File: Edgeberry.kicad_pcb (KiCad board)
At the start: 2 copper layers, 135 x 90 mm, 171 parts, among them J1 Molex_KK_1x02_P2.54mm_CONN, P1 Barrel_Jack_CONN, Q1 BC547, Q2 BC547, Q3 BC547, SW1 SW_PUSH_Horizontal, U1 24LC256, U2 LM2596S-5.0

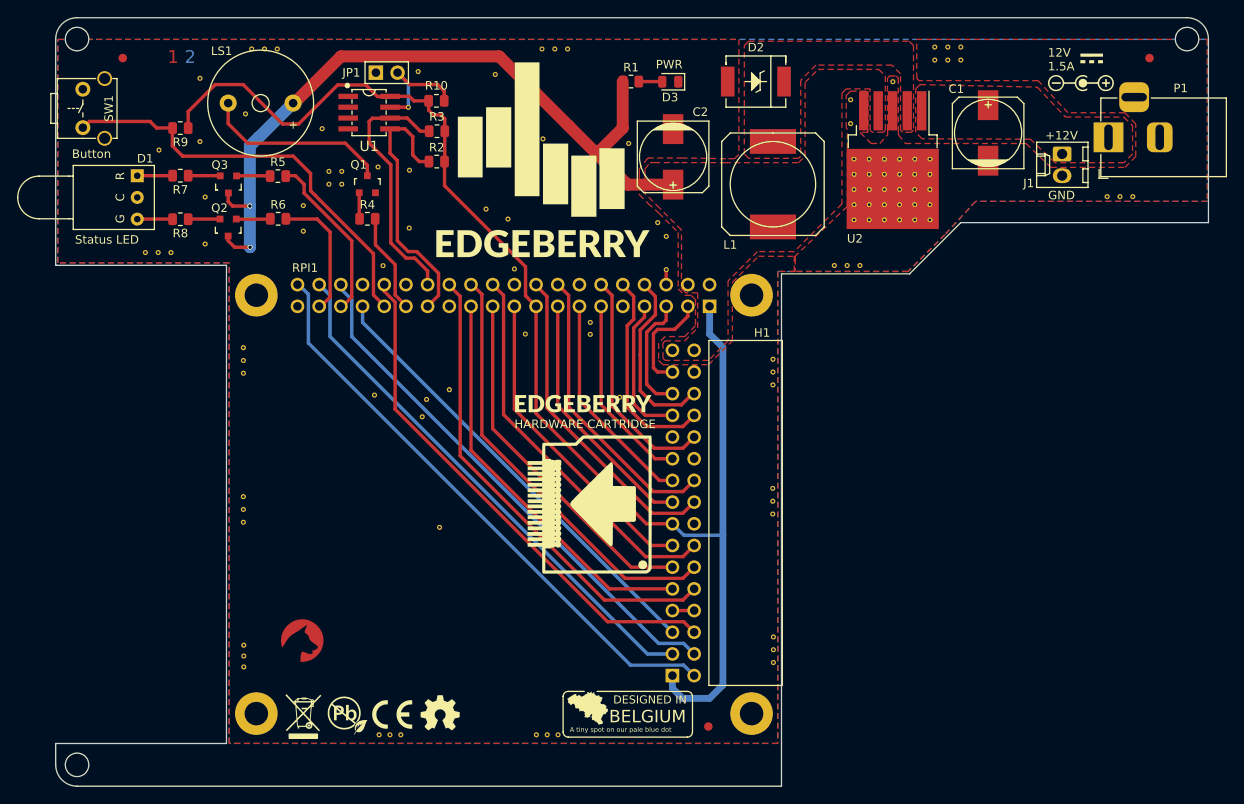
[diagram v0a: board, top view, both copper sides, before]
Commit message: Bugfix RPi footprint + via's are via's now instead footprints. KiCad * update.
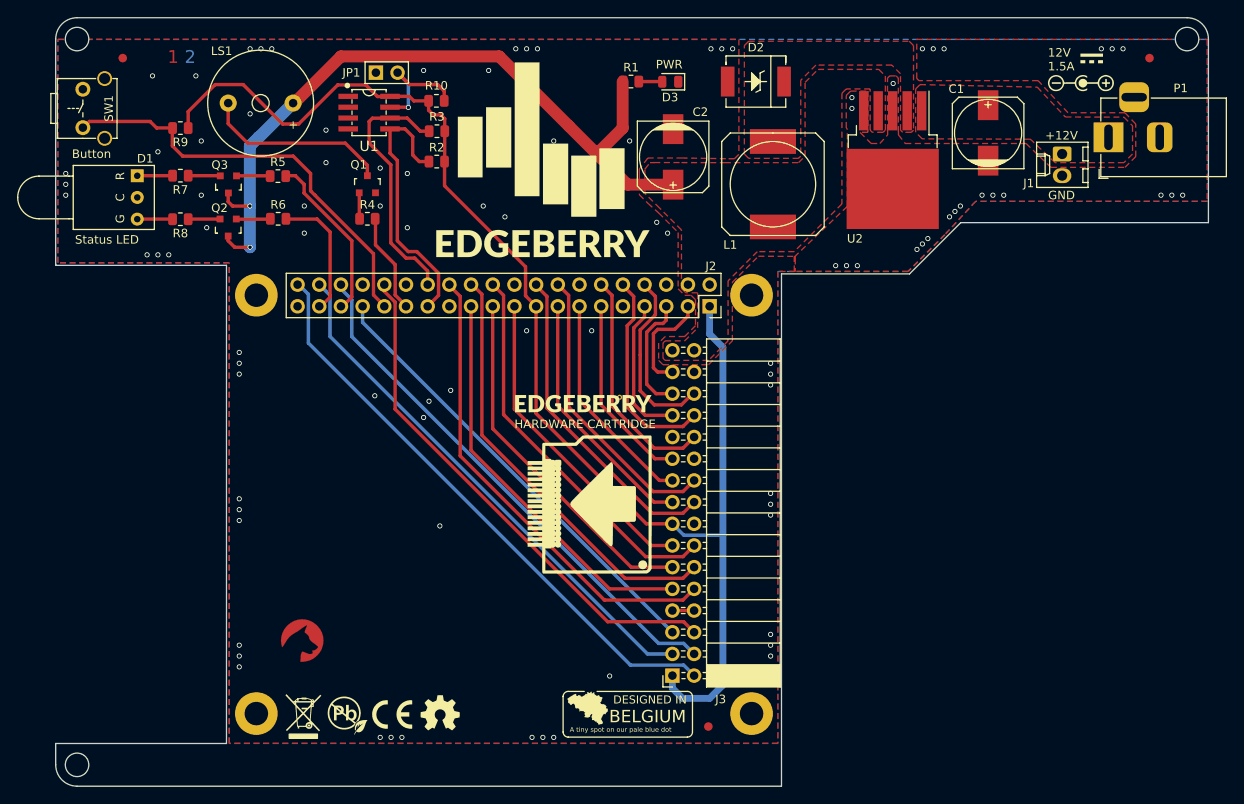
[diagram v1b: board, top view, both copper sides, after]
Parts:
- removed ? (x3): , 
- removed H1: 2X16Pin_P2.54mm_Horizontal_Receptacle_Connector, emcosys:EdgeBerry_IO
- removed the REF** at (114.8, 64.8)
- removed the REF** at (139.9, 135.8)
- removed the REF** at (128.6, 111.5)
- removed the REF** at (115.6, 69.8)
- removed the REF** at (141.2, 135.8)
- removed the REF** at (125.1, 76.4)
- removed the REF** at (121.0, 96.0)
- removed the REF** at (154.1, 75.8)
- removed the REF** at (105.6, 90.4)
- removed the REF** at (177.8, 80.8)
- removed the REF** at (105.6, 109.4)
- removed the REF** at (105.7, 125.3)
- removed the REF** at (105.7, 126.5)
- removed the REF** at (167.7, 127.3)
- removed the REF** at (121.5, 135.8)
- removed the REF** at (124.1, 135.8)
- removed the REF** at (135.1, 58.4)
- removed the REF** at (167.7, 124.3)
- removed the REF** at (105.7, 127.8)
- removed the REF** at (138.6, 88.8)
- removed the REF** at (181.7, 59.3)
- removed the REF** at (167.7, 125.8)
- removed the REF** at (122.8, 135.8)
- removed the REF** at (174.8, 80.8)
- removed the REF** at (105.6, 107.9)
- removed the REF** at (176.3, 80.8)
- removed the REF** at (105.6, 110.9)
- removed the REF** at (112.6, 73.8)
- removed the REF** at (178.9, 73.7)
- removed the REF** at (105.6, 91.9)
- removed the REF** at (178.9, 75.4)
- removed the REF** at (177.1, 70.1)
- removed the REF** at (177.1, 75.4)
- removed the REF** at (180.7, 68.3)
- removed the REF** at (100.5, 58.9)
- removed the REF** at (182.5, 68.3)
- removed the REF** at (176.7, 64.2)
- removed the REF** at (101.1, 78.3)
- removed the REF** at (186.0, 73.7)
- removed the REF** at (177.1, 71.9)
- removed the REF** at (177.1, 73.7)
- removed the REF** at (180.7, 71.9)
- removed the REF** at (186.0, 71.9)
- removed the REF** at (136.6, 75.4)
- removed the REF** at (155.1, 81.3)
- removed the REF** at (184.3, 73.7)
- removed the REF** at (182.5, 70.1)
- removed the REF** at (178.9, 70.1)
- removed the REF** at (182.5, 73.7)
- removed the REF** at (178.9, 68.3)
- removed the REF** at (122.0, 80.8)
- removed the REF** at (180.7, 70.1)
- removed the REF** at (180.7, 75.4)
- removed the REF** at (184.3, 75.4)
- removed the REF** at (117.1, 71.3)
- removed the REF** at (117.1, 69.8)
- removed the REF** at (184.3, 70.1)
- removed the REF** at (178.9, 71.9)
- removed the REF** at (142.1, 55.4)
- removed the REF** at (182.5, 71.9)
- removed the REF** at (209.8, 72.7)
- removed the REF** at (127.1, 96.5)
- removed the REF** at (186.6, 56.7)
- removed the REF** at (176.7, 61.4)
- removed the REF** at (143.6, 55.4)
- removed the REF** at (186.0, 70.1)
- removed the REF** at (109.6, 55.4)
- removed the REF** at (188.1, 56.7)
- removed the REF** at (112.6, 76.8)
- removed the REF** at (146.3, 87.5)
- removed the REF** at (186.0, 68.3)
- removed the REF** at (186.6, 55.2)
- removed the REF** at (208.3, 72.7)
- removed the REF** at (115.6, 71.3)
- removed the REF** at (121.4, 69.3)
- removed the REF** at (189.6, 56.7)
- removed the REF** at (184.3, 68.3)
- removed the REF** at (126.6, 98.5)
- removed the REF** at (146.3, 88.9)
- removed the REF** at (184.3, 71.9)
- removed the REF** at (129.8, 95.3)
- removed the REF** at (95.7, 67.3)
- removed the REF** at (189.6, 55.2)
- removed the REF** at (177.1, 68.3)
- removed the REF** at (188.1, 55.2)
- removed the REF** at (182.5, 75.4)
- removed the REF** at (180.7, 73.7)
- removed the REF** at (186.0, 75.4)
- removed the REF** at (101.1, 72.8)
- removed the REF** at (105.6, 93.4)
- removed the REF** at (167.6, 91.8)
- removed the REF** at (140.6, 55.4)
- removed the REF** at (137.4, 81.2)
- removed the REF** at (94.1, 79.3)
- removed the REF** at (95.6, 79.3)
- removed the REF** at (140.7, 66.0)
- removed the REF** at (206.8, 72.7)
- removed the REF** at (100.5, 66.3)
- removed the REF** at (167.6, 108.4)
- removed the REF** at (167.6, 106.9)
- removed the REF** at (167.6, 109.9)
- removed the REF** at (97.1, 79.3)
- removed the REF** at (167.6, 94.8)
- removed the REF** at (167.6, 93.3)
- removed the REF** at (105.9, 63.0)
- removed the REF** at (142.5, 135.8)
- removed the REF** at (106.6, 55.4)
- removed the REF** at (108.1, 55.4)
- removed the REF** at (125.1, 69.6)
- removed the REF** at (155.2, 77.4)
- removed the REF** at (134.0, 74.2)
- removed RPI1: 2X20Pin_2.54mm_Receptacle_CONN, emcosys:RPI_GPIO
- added J2: Raspberry_Pi_2_3, Connector_PinSocket_2.54mm:PinSocket_2x20_P2.54mm_Vertical, F.Cu at (160.2, 85.6)
- added J3: Edgeberry Cartridge Connector, Connector_PinSocket_2.54mm:PinSocket_2x16_P2.54mm_Horizontal, F.Cu at (155.9, 128.8)
- J1: value Molex_KK_1x02_P2.54mm_CONN -> Molex_KK_1x02_P2.54mm
- P1: value Barrel_Jack_CONN -> 12Vin
- SW1: value SW_PUSH_Horizontal -> SW_PUSH
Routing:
- net GND: track 5.50 -> 2.54 mm, vias 0 -> 94
- net GPIO_27: track 26.5 -> 25.8 mm
- net GPIO_22: track 30.4 -> 29.8 mm
- net LED_red: track 20.3 -> 19.8 mm
- net LED_green: track 15.7 -> 15.2 mm
- net WP: vias 0 -> 1
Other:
- board text added: "REV 1.5"
- board text added: "REV.: 1.5, Mid 2024"
- board text removed: "REV 1.4"
- board text removed: "REV.: 1.4, Mid 2024"

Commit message: Open Source Hardware license: CERN-OHL-W
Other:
- board text added: "Copyright© 2024 Sanne 'SpuQ' Santens. This design is released under the CERN OHL-W license on GitHub."
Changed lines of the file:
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@@
 		)
 		(fp_text user "${REFERENCE}"
-			(at -8.315 19.05 270)
+			(at -8.315 19.05 -90)
 			(layer "F.Fab")
 			(effects
@@
 	)
 	(gr_text "Edgeberry Hardware"
-		(at 72.449 29.072 0)
+		(at 72.449 19.772 0)
 		(layer "Dwgs.User")
 		(effects
@@
 	)
 	(gr_text "REV.: 1.5, Mid 2024"
-		(at 72.949 36.572 0)
+		(at 72.949 26.772 0)
 		(layer "Dwgs.User")
 		(effects
@@
 		)
 	)
+	(gr_text "Copyright© 2024 Sanne 'SpuQ' Santens. This design is released under\nthe CERN OHL-W license on GitHub."
+		(at 73.309 33.772 0)
+		(layer "Dwgs.User")
+		(effects
+			(font
+				(size 1.5 1.5)
+				(thickness 0.2)
+				(bold yes)
+			)
+			(justify left bottom)
+		)
+	)

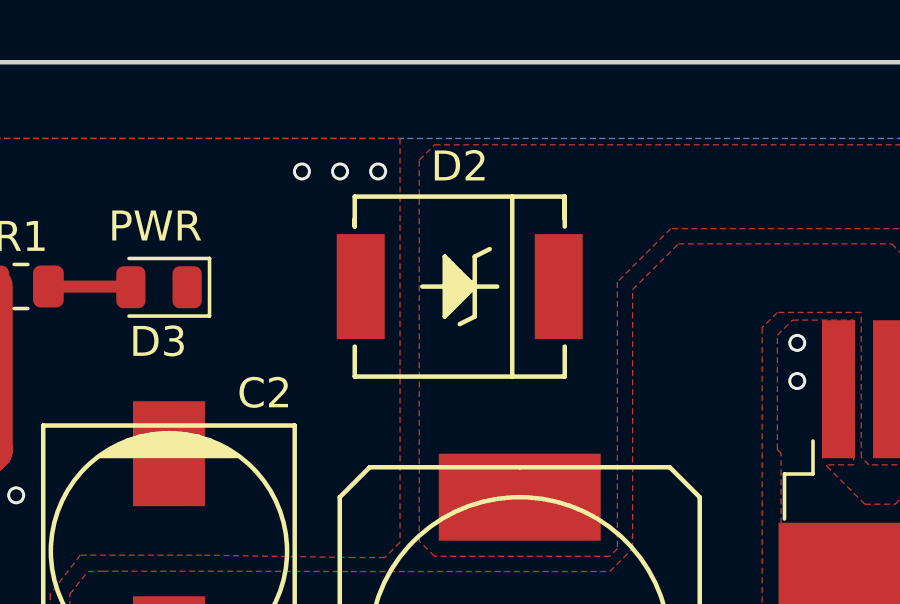
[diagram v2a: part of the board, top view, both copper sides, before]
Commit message: Buck convertor: Schottky diode footprint modification
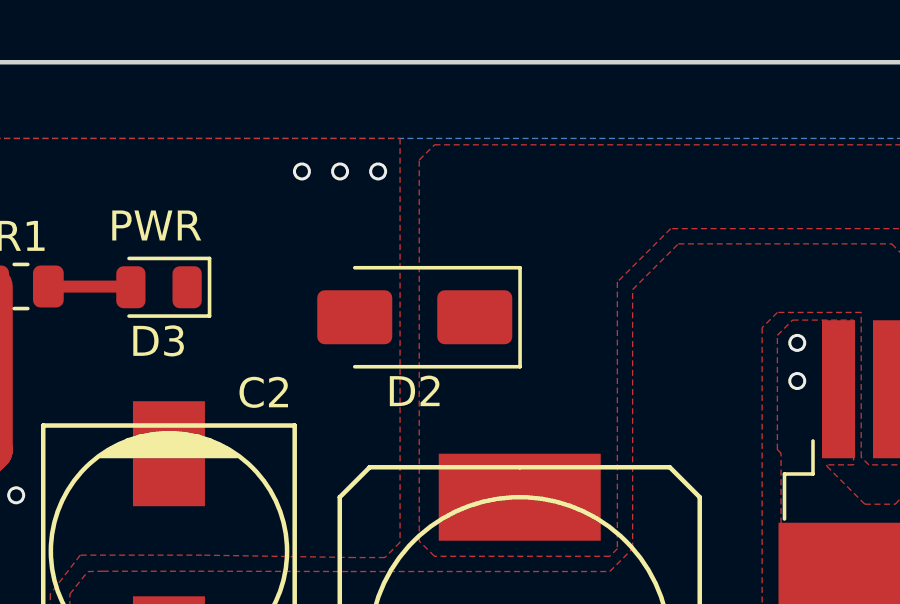
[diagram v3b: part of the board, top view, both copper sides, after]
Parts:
- D2: footprint emcosys:SS54_Schottky_40V_5A -> Diode_SMD:D_SMA
- moved D2 1.82 mm to (164.1, 60.3), turned to 180 degrees
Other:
- board text added: "REV 1.6"
- board text added: "REV.: 1.6, Mid 2024"
- board text removed: "REV 1.5"
- board text removed: "REV.: 1.5, Mid 2024"

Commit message: Edgeberry rev1.7
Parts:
- moved REF** 1.70 mm to (87.9, 21.7)
- moved G*** 1.10 mm to (206.0, 56.6)
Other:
- board text added: "12-24V 1.5A"
- board text added: "Base Board Rev. 1.7, late 2024"
- board text added: "EDGEBERRY"
- board text added: "REV 1.7"
- board text added: "V+"
- board text removed: "+12V"
- board text removed: "12V 1.5A"
- board text removed: "Edgeberry Hardware"
- board text removed: "REV 1.6"
- board text removed: "REV.: 1.6, Mid 2024"
